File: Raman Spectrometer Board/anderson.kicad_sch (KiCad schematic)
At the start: 1 part

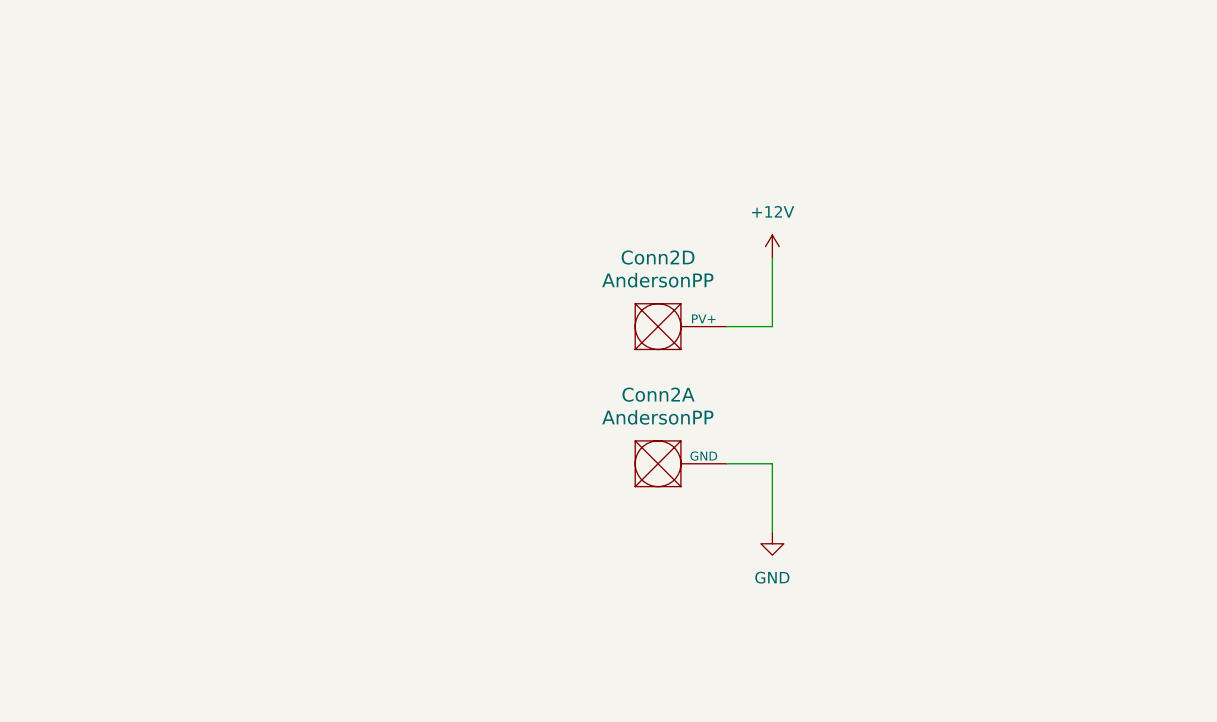
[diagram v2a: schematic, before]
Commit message: Gantry Motor Andersons Added
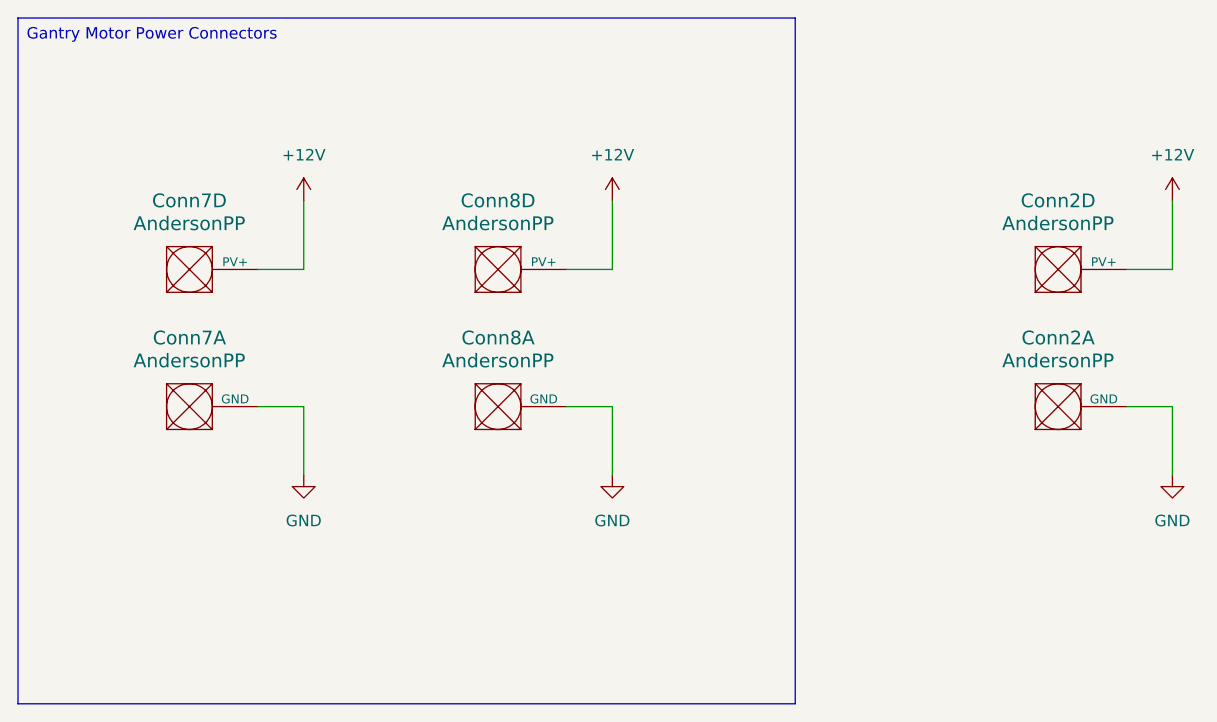
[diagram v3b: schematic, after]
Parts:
- added Conn7, Conn8: AndersonPP, symbol MRDT_Connectors:AndersonPP
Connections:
- net +12V: now also Conn7.4 (PV+), Conn8.4 (PV+)
- net GND: now also Conn7.1 (GND), Conn8.1 (GND)
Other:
- moved on the sheet: Conn2A, Conn2D

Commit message: Added footprints to main board
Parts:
- Conn2, Conn7, Conn8: footprint (none) -> MRDT_Connectors:Anderson_2_Horizontal_Side_by_Side_PV
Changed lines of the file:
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@@
 			)
 		)
-		(property "Footprint" ""
+		(property "Footprint" "MRDT_Connectors:Anderson_2_Horizontal_Side_by_Side_PV"
 			(at 91.44 100.33 0)
 			(effects
@@
 			)
 		)
-		(property "Footprint" ""
+		(property "Footprint" "MRDT_Connectors:Anderson_2_Horizontal_Side_by_Side_PV"
 			(at 125.73 100.33 0)
 			(effects
@@
 			)
 		)
-		(property "Footprint" ""
+		(property "Footprint" "MRDT_Connectors:Anderson_2_Horizontal_Side_by_Side_PV"
 			(at 187.96 100.33 0)
 			(effects
@@
 			)
 		)
-		(property "Footprint" ""
+		(property "Footprint" "MRDT_Connectors:Anderson_2_Horizontal_Side_by_Side_PV"
 			(at 187.96 115.57 0)
 			(effects
@@
 			)
 		)
-		(property "Footprint" ""
+		(property "Footprint" "MRDT_Connectors:Anderson_2_Horizontal_Side_by_Side_PV"
 			(at 125.73 115.57 0)
 			(effects
@@
 			)
 		)
-		(property "Footprint" ""
+		(property "Footprint" "MRDT_Connectors:Anderson_2_Horizontal_Side_by_Side_PV"
 			(at 91.44 115.57 0)
 			(effects

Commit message: tof voltages connected
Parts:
- Conn2, Conn7, Conn8: footprint MRDT_Connectors:Anderson_2_Horizontal_Side_by_Side_PV -> (none)
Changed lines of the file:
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@@
 			)
 		)
-		(property "Footprint" "MRDT_Connectors:Anderson_2_Horizontal_Side_by_Side_PV"
+		(property "Footprint" ""
 			(at 91.44 100.33 0)
 			(effects
@@
 			)
 		)
-		(property "Footprint" "MRDT_Connectors:Anderson_2_Horizontal_Side_by_Side_PV"
+		(property "Footprint" ""
 			(at 125.73 100.33 0)
 			(effects
@@
 			)
 		)
-		(property "Footprint" "MRDT_Connectors:Anderson_2_Horizontal_Side_by_Side_PV"
+		(property "Footprint" ""
 			(at 187.96 100.33 0)
 			(effects
@@
 			)
 		)
-		(property "Footprint" "MRDT_Connectors:Anderson_2_Horizontal_Side_by_Side_PV"
+		(property "Footprint" ""
 			(at 187.96 115.57 0)
 			(effects
@@
 			)
 		)
-		(property "Footprint" "MRDT_Connectors:Anderson_2_Horizontal_Side_by_Side_PV"
+		(property "Footprint" ""
 			(at 125.73 115.57 0)
 			(effects
@@
 			)
 		)
-		(property "Footprint" "MRDT_Connectors:Anderson_2_Horizontal_Side_by_Side_PV"
+		(property "Footprint" ""
 			(at 91.44 115.57 0)
 			(effects
